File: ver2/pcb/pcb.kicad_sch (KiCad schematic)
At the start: 142 parts, among them M1 Ezurio BL54L15 (nrf54L15) mod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, SW1 SW_DIP_x01

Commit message: A  bak/README.md R  ver2/RP2040_Minimal.kicad_sym -> bak/RP2040_Minimal.kicad_sym A  bak/border.py A  bak/dumploc.py A  bak/nordic-lib-kicad-npm.kicad_sym A  bak/pcb/LED.kicad_sch R  ver2/pcb/dxf/pcb-Edge_Cuts.dxf -> bak/pcb/dxf/pcb-Edge_Cuts.dxf A  bak/pcb/fp-lib-table A  bak/pcb/pcb.kicad_pcb A  bak/pcb/pcb.kicad_prl A  bak/pcb/pcb.kicad_pro A  bak/pcb/pcb.kicad_sch A  bak/pcb/switch.kicad_sch A  bak/pcb/sym-lib-table A  bak/placefp.py R  ver2/plate/dxf/plate-Edge_Cuts.dxf -> bak/plate/dxf/plate-Edge_Cuts.dxf A  bak/plate/fp-lib-table A  bak/plate/plate.kicad_pcb A  bak/plate/plate.kicad_prl A  bak/plate/plate.kicad_pro A  bak/plate/plate.kicad_sch A  bak/plate/sym-lib-table A  bak/rmtracks.py A  bak/tmr-footprints/Button_Switch_3x4x2.5.kicad_mod A  bak/tmr-footprints/C_0402_1005Metric.kicad_mod A  bak/tmr-footprints/C_0603_1608Metric.kicad_mod A  bak/tmr-footprints/DFN-3L-1.6x1.6.kicad_mod A  bak/tmr-footprints/Ezurio_BL54L15_Module.kicad_mod A  bak/tmr-footprints/Gateron_Switch_Lowpro.kicad_mod A  bak/tmr-footprints/IS31FL3731-RECESSED-SSOP-28_5.3x10.2mm_P0.65mm.kicad_mod A  bak/tmr-footprints/IS31FL3731-SSOP-28_5.3x10.2mm_P0.65mm.kicad_mod A  bak/tmr-footprints/JLC_Order_Num.kicad_mod A  bak/tmr-footprints/LED-6028.kicad_mod A  bak/tmr-footprints/LED_1206_3216Metric_ReverseMount_Hole2.1mm.kicad_mod A  bak/tmr-footprints/LED_1206_3216Metric_ReverseMount_Hole2.2x1.8mm.kicad_mod A  bak/tmr-footprints/L_Samsung_CIGT201610EH2R2MNE.kicad_mod A  bak/tmr-footprints/MCP3208-RECESSED-SOIC-16_3.9x9.9mm_P1.27mm.kicad_mod A  bak/tmr-footprints/MCP3208-SOIC-16_3.9x9.9mm_P1.27mm.kicad_mod R  ver2/tmr-footprints/MountingHole_1.6mm.kicad_mod -> bak/tmr-footprints/MountingHole_1.6mm.kicad_mod A  bak/tmr-footprints/MountingHole_2.1mm_M2_NoPad.kicad_mod A  bak/tmr-footprints/MountingHole_2.2mm_M2_NoPad.kicad_mod A  bak/tmr-footprints/MountingHole_5.3mm_M5_ISO14580_Pad_TopBottom.kicad_mod A  bak/tmr-footprints/Panasonic_EVPAE.kicad_mod A  bak/tmr-footprints/R_0402_1005Metric.kicad_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
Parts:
- removed JTAG1: Conn_02x05_Odd_Even, tmr-lib:SAMTEC-CLP-105-02-X-D-A, symbol Connector_Generic:Conn_02x05_Odd_Even
- removed JTAG2: Conn_02x05_Odd_Even, Connector:Tag-Connect_TC2050-IDC-NL_2x05_P1.27mm_Vertical, symbol Connector_Generic:Conn_02x05_Odd_Even
- removed M1: Ezurio BL54L15 (nrf54L15) module, tmr-lib:Ezurio_BL54L15_Module, symbol tmr-lib:Ezurio_BL54L15_TRACE ANT_SCH_Symbol
- removed USB1: USB_C_Receptacle_PowerOnly_6P, Connector_USB:USB_C_Receptacle_GCT_USB4125-xx-x-0190_6P_TopMnt_Horizontal, symbol Connector:USB_C_Receptacle_PowerOnly_6P
- added BAT2: ~, Connector_JST:JST_SH_SM03B-SRSS-TB_1x03-1MP_P1.00mm_Horizontal, symbol tmr-lib:Battery_Pack_PS5
- added C1, C3: 10uF, Capacitor_SMD:C_0603_1608Metric, symbol Device:C_Small
- added C2, C4: 12pF, tmr-lib:C_0402_1005Metric, symbol Device:C_Small
- added Hs12: M2_Pad, MountingHole:MountingHole_2.2mm_M2_ISO7380_Pad_TopBottom, symbol Mechanical:MountingHole
- added JTAG1: Conn_ARM_JTAG_SWD_10, tmr-lib:SAMTEC-CLP-105-02-X-D-A, symbol Connector:Conn_ARM_JTAG_SWD_10
- added JTAG2: Conn_ARM_JTAG_SWD_10, Connector:Tag-Connect_TC2050-IDC-NL_2x05_P1.27mm_Vertical, symbol Connector:Conn_ARM_JTAG_SWD_10
- added Jusb1: USB_TYPE_C_Receptacle_16P, Connector_USB:USB_C_Receptacle_XKB_U262-16XN-4BVC11, symbol tmr-lib:USB_TYPE_C_Receptacle_16P
- added MDBT1: ~, RF_Module:Raytac_MDBT50Q, symbol pcb-eagle-import:MDBT50
- added R1, R2: 27R, tmr-lib:R_0603_1608Metric, symbol Device:R_Small
- added Y1: 32.768 kHz, Crystal:Crystal_SMD_2012-2Pin_2.0x1.2mm, symbol Device:Crystal_Small
- renumbered C6 to C10, C7 to C11, C8 to C12, C9 to C13, C10 to C14, C11 to C15, C12 to C16, C13 to C17, C15 to C18, C14 to C19, C16 to C20, C17 to C21, C18 to C22, C19 to C23, C20 to C24, C21 to C25, C22 to C26, C23 to C27, C24 to C28, C25 to C29, C26 to C30, C27 to C31, C28 to C32, C29 to C33, C30 to C34, C31 to C35, C32 to C36, C1 to C5, C2 to C6, C3 to C7, C4 to C8, C5 to C9, R1 to R3, R2 to R4, R3 to R5, R4 to R6, PMIC1 to U1
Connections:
- net AIN0: now also MDBT1.11 (P0.02/AIN0)
- net AIN1: now also MDBT1.9 (P0.03/AIN1)
- net AIN2: now also MUXA1.12 (D4), MDBT1.20 (P0.04/AIN2); no longer MUXA1.9 (D3)
- net AIN3: now also MUXA1.9 (D3), MDBT1.21 (P0.05/AIN3); no longer MUXA1.12 (D4)
- net AIN4: now also MUXA2.7 (D2), MDBT1.13 (P0.28/AIN4); no longer MUXA2.9 (D3)
- net AIN5: now also MUXA2.9 (D3), MDBT1.10 (P0.29/AIN5); no longer MUXA2.12 (D4)
- net AIN6: now also MDBT1.14 (P0.30/AIN6)
- net AIN7: now also MUXA2.12 (D4), MDBT1.12 (P0.31/AIN7); no longer MUXA2.7 (D2)
- net GND: now also BAT2.3 (GND), C1.2, C2.2, C3.2, C4.2, JTAG1.3 (GND), JTAG1.5 (GND), JTAG1.9 (GNDDetect), JTAG2.3 (GND), JTAG2.5 (GND), JTAG2.9 (GNDDetect), Jusb1.A1 (GND), Jusb1.A12 (GND), Jusb1.B1 (GND), Jusb1.B12 (GND), Jusb1.S1 (SHIELD), MDBT1.1 (GND@1), MDBT1.15 (GND@15), MDBT1.2 (GND@2), MDBT1.33 (GND@33), MDBT1.55 (GND@55)
- net GPIO_X: now also MDBT1.38 (P0.16)
- net INT: now also MDBT1.36 (P0.14)
- net LED_DR_EN: now also MDBT1.37 (P0.13)
- net LOADSW_CTRL: now also MDBT1.39 (P0.15)
- net MUXA_SEL: now also MDBT1.41 (P0.17)
- net MUXB_SEL_0: now also MDBT1.22 (P0.06)
- net MUXB_SEL_1: now also MDBT1.23 (P0.07)
- net MUXB_SEL_2: now also MDBT1.25 (P1.08)
- net NRESET: now also JTAG1.10 (~{RESET}), JTAG2.10 (~{RESET}), MDBT1.40 (P0.18/RESET)
- net SCL: now also MDBT1.27 (P0.11)
- net SDA: now also MDBT1.29 (P0.12)
- net SWDCLK: now also JTAG1.4 (SWCLK/TCK), JTAG2.4 (SWCLK/TCK), MDBT1.53 (SWDCLK)
- net SWDIO: now also JTAG1.2 (SWDIO/TMS), JTAG2.2 (SWDIO/TMS), MDBT1.51 (SWDIO)
- net VDDIO: now also C3.1, JTAG1.1 (VTref), JTAG2.1 (VTref), MDBT1.28 (VDD), MDBT1.30 (VDDH)
- net VBUSOUT: now reaches C19.1, U1.22 (VBUSOUT)
- net VBUSOUT: now also C1.1, MDBT1.32 (VBUS)
- net at U1.23 (CC1): now also Jusb1.A5 (CC1)
- net at C18.1, U1.21 (VBUS): now also Jusb1.A4 (VBUS), Jusb1.A9 (VBUS), Jusb1.B4 (VBUS), Jusb1.B9 (VBUS)
- net at U1.24 (CC2): now also Jusb1.B5 (CC2)
- net VBAT: now reaches BAT1.1 (VBAT), C32.1, U1.19 (VBAT)
- net VBAT: now also BAT2.1 (VBAT)
- new net: C4.1, MDBT1.18 (P0.01/XL2), Y1.2
- new net: C2.1, MDBT1.17 (P0.00/XL1), Y1.1
- new net: MDBT1.34 (D-), R2.1
- new net: MDBT1.35 (D+), R1.1
- new net USB_D+: Jusb1.A6 (D1+), Jusb1.B6 (D2+), R1.2
- new net USB_D-: Jusb1.A7 (D1-), Jusb1.B7 (D2-), R2.2
- no-connect marks 26 -> 40
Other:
- note added: "JTAG"
- note added: "NOTE: - The Mux Placement: Place the 5 muxes as close to the nRF54L15 as possible. It is better to have long traces for the TMR outputs (which are slow DC signals) than long traces for the Mux-to-ADC lines (which carry the "chosen" signal). - Route the analog traces far away from PWM traces."
- note added: "NOTE: Charge current limit (ICHG) must be set by writing to registers BCHGISETMSB and BCHGISETLSB of npm1300. Interrupt line from npm1300 indicates when port detection (whether 500mA port or higher) is complete."
- note removed: "NOTE: - Star Power: Run the 2.1V power from the TPS22902 VOUT to the sensors in a "star" or "tree" pattern, rather than one long daisy chain. This prevents the sensors at the end of the line from seeing a different voltage than the sensors at the start. - The Mux Placement: Place the 5 muxes as close to the nRF54L15 as possible. It is better to have long traces for the TMR outputs (which are slow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"
- moved on the sheet: C18

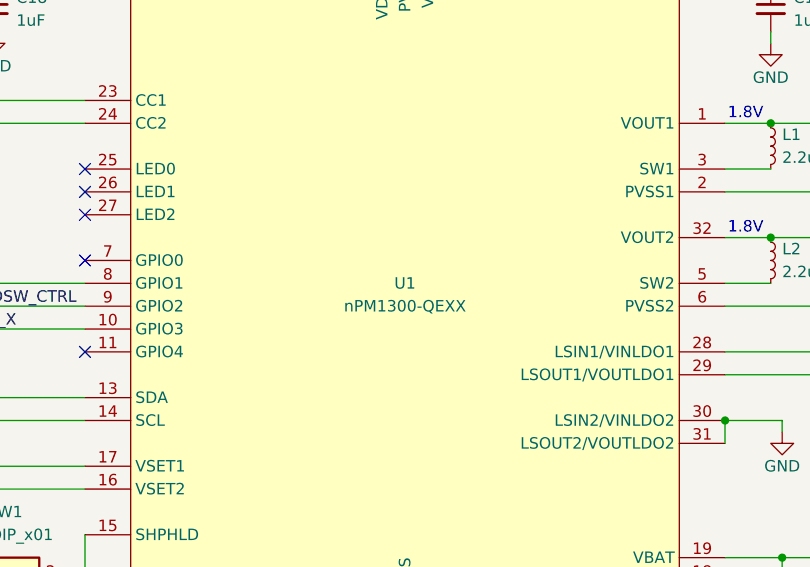
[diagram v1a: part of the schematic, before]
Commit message: M  ver2/border.py M  ver2/pcb/pcb.kicad_pcb M  ver2/pcb/pcb.kicad_sch M  ver2/placefp.py M  ver3/border.py
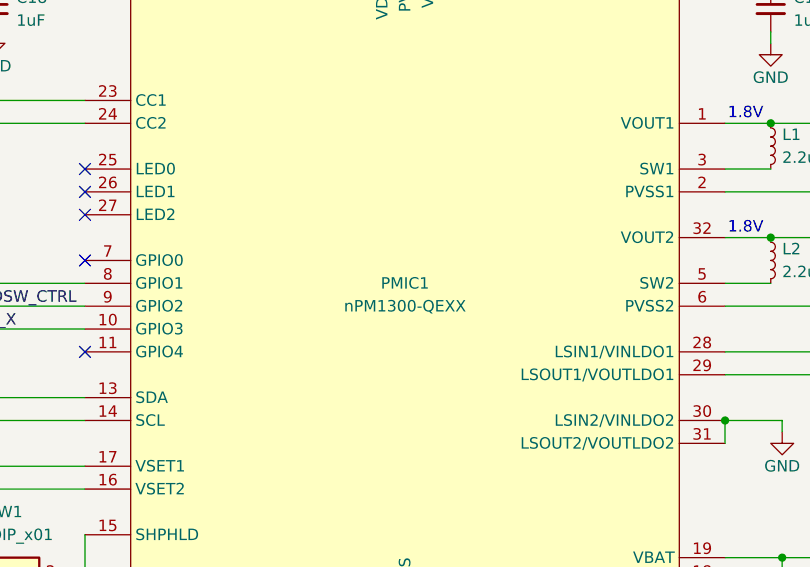
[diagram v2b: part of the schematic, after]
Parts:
- renumbered U1 to PMIC1
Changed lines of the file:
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@@
 		(dnp no)
 		(fields_autoplaced yes)
-		(property "Reference" "U1"
+		(property "Reference" "PMIC1"
 			(at 440.69 275.59 0)
 			(do_not_autoplace yes)
@@
 			(project ""
 				(path "/672ae9a0-2ac9-4023-9977-e9626ff99f32"
-					(reference "U1")
+					(reference "PMIC1")
 					(unit 1)
 				)
